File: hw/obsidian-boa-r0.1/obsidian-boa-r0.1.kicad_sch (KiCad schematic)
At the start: 79 parts, among them J1 USB_C, J2 PROG, P0 0, P1 1, P10 10, P11 11, P12 12, P13 13, P14 14, P15 15, P16 16, P17 17, P18 18, P19 19, P2 2, P20 20, P21 21, P22 22, P23 23, P24 GND, P25 GND, P26 GND, P27 3V3, P28 3V3, P29 VIN, P3 3, P30 CDONE, P31 CRESET, P32 UP, P33 UP, P34 UP, P35 UP, P4 4, P5 5, P6 6, P7 7, P8 8, P9 9, SW1 TACT, U1 USBLC6-2, U2 W25Q32JVSS, U3 ESP32-S2, U4 W25Q32JVSS, U5 TPS62290, Y1 40MHz

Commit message: hw.r0d1: Tidy up schematic, plan out layout on PCB
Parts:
- removed JP5: Jumper, pkl_jumpers:J_NC_0603_30, symbol icebreaker-bitsy-rescue:pkl_jumper_nc-pkl_misc
- removed R6: 1k5, pkl_dipol:R_0402, symbol icebreaker-bitsy-rescue:pkl_R_Small-pkl_device
- removed R9: 10k, pkl_dipol:R_Array_Convex_4x0402, symbol icebreaker-bitsy-rescue:pkl_R4_Small-pkl_device
- removed RN1: R_Network04_Split, Resistor_SMD:R_Array_Convex_4x0402, symbol Device:R_Network04_Split
- added C13, C15: 100n, Capacitor_SMD:C_0402_1005Metric, symbol icebreaker-bitsy-rescue:pkl_C_Small-pkl_device
- added C14, C8: 10u, Capacitor_SMD:C_0603_1608Metric, symbol icebreaker-bitsy-rescue:pkl_C-pkl_device
- added FB1, FB2, FB3: 240R, Inductor_SMD:L_0402_1005Metric, symbol Device:Ferrite_Bead_Small
- added L2: L_Small, Inductor_SMD:L_0402_1005Metric, symbol Device:L_Small
- added RN1: 10k, Resistor_SMD:R_Array_Convex_4x0402, symbol Device:R_Pack04_Split
- C1, C12, C2, C3, C4, C9: footprint pkl_dipol:C_0402 -> Capacitor_SMD:C_0402_1005Metric
- C10, C11: value 100n -> TBD; footprint pkl_dipol:C_0402 -> Capacitor_SMD:C_0402_1005Metric
- C19: footprint pkl_dipol:C_0603 -> Capacitor_SMD:C_0603_1608Metric
- D1, D2, D3: footprint pkl_dipol:D_0603 -> obsidian-boa:LED_0603_1608Metric_Compact; symbol icebreaker-bitsy-rescue:pkl_Led_Small-pkl_device -> Device:LED_ALT
- JP1: footprint pkl_jumpers:J_NC_0603_40 -> Jumper:SolderJumper-2_P1.3mm_Bridged2Bar_RoundedPad1.0x1.5mm
- R1, R10, R11, R12, R13, R2, R3, R4, R5: footprint pkl_dipol:R_0402 -> Resistor_SMD:R_0402_1005Metric
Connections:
- net VCCIO_0 is gone; now on an unnamed net: C10.1
- net VCCIO_2 is gone; now on net +3V3: R10.2
- net +3V3: now also FB1.1, FB2.1, FB3.1, RN1.5 (R4.2), RN1.6 (R3.2), RN1.7 (R2.2), RN1.8 (R1.2); no longer C11.1, C19.1, C9.1, U3.1 (VDDA), U3.20 (VDD3P3_RTC), U3.27 (VDD3P3_RTC_IO), U3.3 (VDD3P3), U3.30 (VDD_SPI), U3.4 (VDD3P3), U3.45 (VDD3P3_CPU), U3.51 (VDDA), U3.54 (VDDA)
- net CDONE: no longer D3.A, R13.1
- net GND: now also Y1.2, Y1.4, C13.2, C14.2, C15.2, C8.2; no longer D3.C
- net IOB_13b-~LEDG: now also D2.1 (K); no longer D2.C
- net IOT_36b-~LEDR: now also D1.1 (K); no longer D1.C
- net RAM_~CS: now also RN1.2 (R2.1)
- net SPI_SCK: now also RN1.3 (R3.1)
- net SPI_~CS: now also RN1.1 (R1.1)
- net USB_N: now also U3.25 (GPIO19)
- net USB_P: now also U3.26 (GPIO20)
- net ~CRESET: now also RN1.4 (R4.1)
- net at R12.1: now also D2.2 (A); no longer D2.A
- net at R11.1: now also D1.2 (A); no longer D1.A
- net at U3.2 (LNA_IN): now also L2.1
- net at AE1.1 (A): now also C11.1, L2.2
- new net: C19.1, C9.1, FB1.2, U3.20 (VDD3P3_RTC), U3.27 (VDD3P3_RTC_IO), U3.30 (VDD_SPI), U3.45 (VDD3P3_CPU)
- new net: D3.2 (A), R13.1
- new net: C13.1, C8.1, FB3.2, U3.1 (VDDA), U3.51 (VDDA), U3.54 (VDDA)
- new net: C14.1, C15.1, FB2.2, U3.3 (VDD3P3), U3.4 (VDD3P3)
- new net IOB_13b-~LEDB: D3.1 (K)
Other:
- note removed: "3V3 VReg"
- note removed: "Using same values as STM32F1 spec"
- moved on the sheet: AE1, C12, C19, C3, C4, C9, R11, R12, R13, R4, R5, Y1

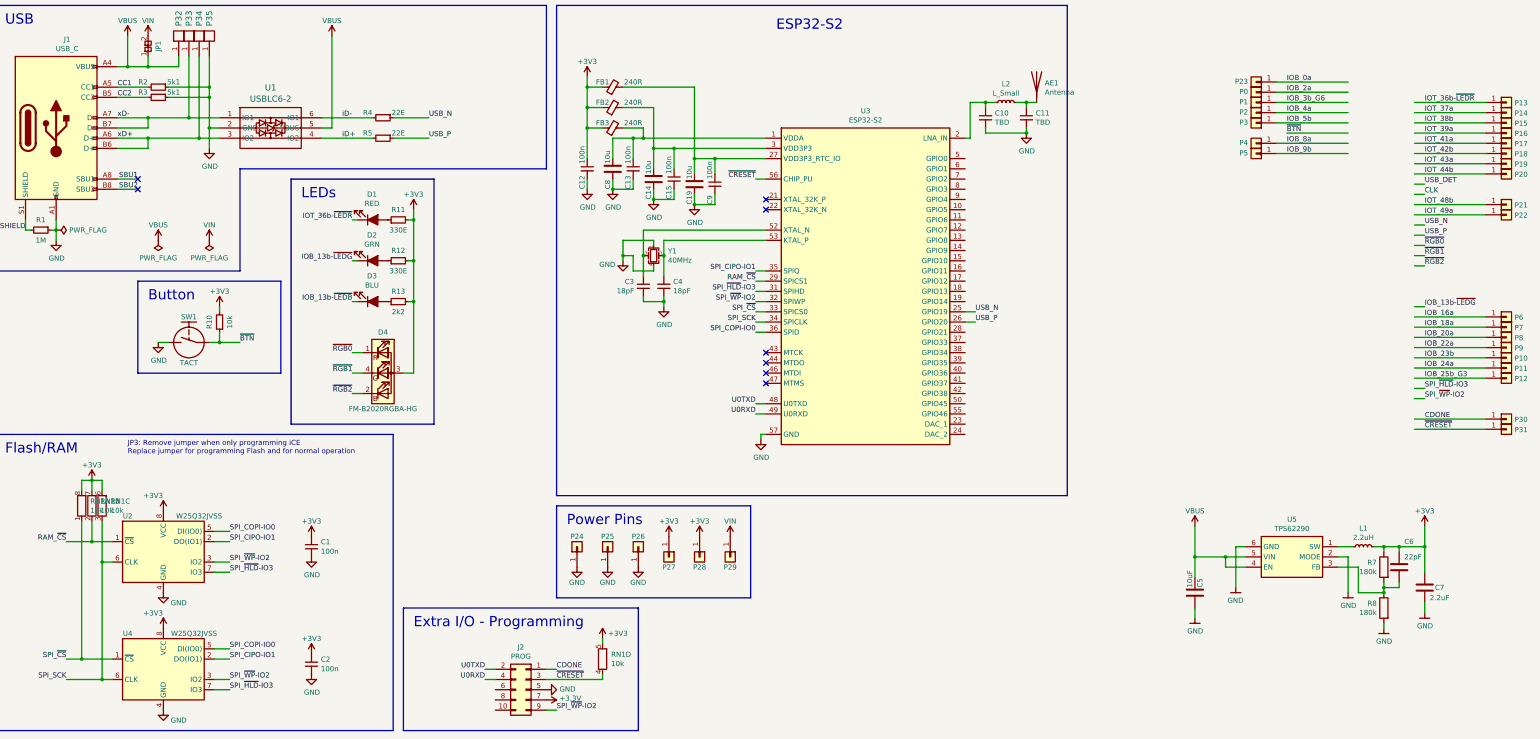
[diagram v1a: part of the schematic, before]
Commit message: hw.r0d1: Update routing and layout
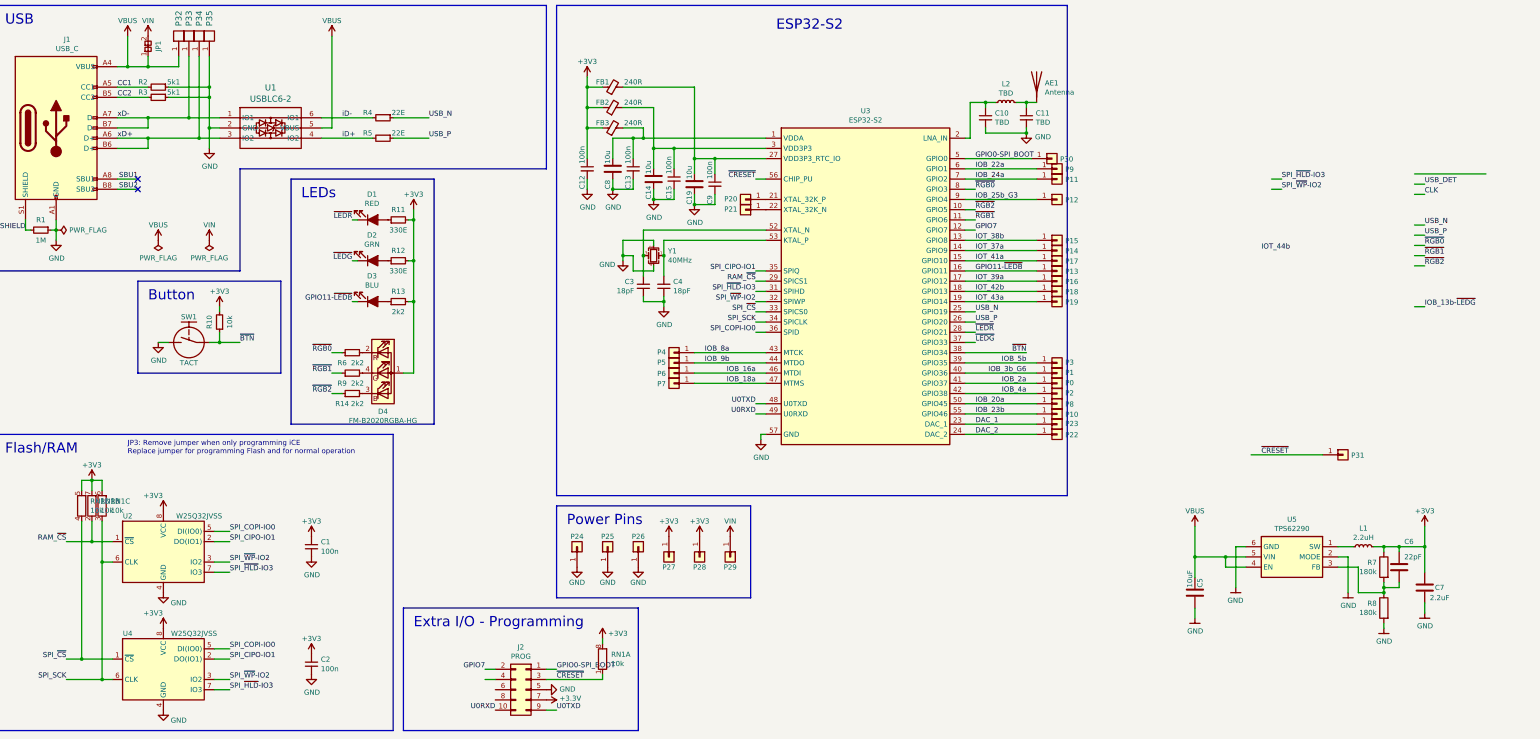
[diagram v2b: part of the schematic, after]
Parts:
- added R14, R6, R9: 2k2, Resistor_SMD:R_0402_1005Metric, symbol icebreaker-bitsy-rescue:pkl_R_Small-pkl_device
- D4: footprint pkl_led:LED_TRI_2020 -> LED_SMD:LED_Lumex_SML-LX0303SIUPGUSB; symbol icebreaker-bitsy-rescue:pkl_LED_RBAG-pkl_device -> Device:LED_ARBG
- L2: value L_Small -> TBD
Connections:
- net CDONE is gone; now on net GPIO0-SPI_BOOT: J2.1 (Pin_1), P30.1 (Pin_1)
- net IOB_0a is gone; now on net DAC_1: P23.1 (Pin_1)
- net IOB_13b-~LEDB is gone; now on net GPIO11-~LEDB: D3.1 (K)
- net IOT_48b is gone; now on an unnamed net: P21.1 (Pin_1)
- net IOT_49a is gone; now on net DAC_2: P22.1 (Pin_1)
- net +3V3: now also D4.1 (A); no longer D4.3 (A)
- net IOB_13b-~LEDG: no longer D2.1 (K)
- net IOB_16a: now also U3.46 (MTDI)
- net IOB_18a: now also U3.47 (MTMS)
- net IOB_20a: now also U3.50 (GPIO45)
- net IOB_22a: now also U3.6 (GPIO1)
- net IOB_23b: now also U3.55 (GPIO46)
- net IOB_24a: now also U3.7 (GPIO2)
- net IOB_25b_G3: now also U3.9 (GPIO4)
- net IOB_2a: now also U3.41 (GPIO37)
- net IOB_3b_G6: now also U3.40 (GPIO36)
- net IOB_4a: now also U3.42 (GPIO38)
- net IOB_5b: now also U3.39 (GPIO35)
- net IOB_8a: now also U3.43 (MTCK)
- net IOB_9b: now also U3.44 (MTDO)
- net IOT_37a: now also U3.14 (GPIO9)
- net IOT_38b: now also U3.13 (GPIO8)
- net IOT_39a: now also U3.17 (GPIO12)
- net IOT_41a: now also U3.15 (GPIO10)
- net IOT_42b: now also U3.18 (GPIO13)
- net IOT_43a: now also U3.19 (GPIO14)
- net IOT_44b: no longer P20.1 (Pin_1)
- net SPI_~CS: now also RN1.4 (R4.1); no longer RN1.1 (R1.1)
- net SPI_~WP~-IO2: no longer J2.9 (Pin_9)
- net U0RXD: now also J2.10 (Pin_10); no longer J2.4 (Pin_4)
- net U0TXD: now also J2.9 (Pin_9); no longer J2.2 (Pin_2)
- net ~BTN: now also U3.38 (GPIO34)
- net ~CRESET: now also RN1.1 (R1.1); no longer RN1.4 (R4.1)
- net ~RGB0: now also U3.8 (GPIO3), R6.1; no longer D4.1 (RK)
- net ~RGB1: now also U3.11 (GPIO6), R9.1; no longer D4.4 (GK)
- net ~RGB2: now also U3.10 (GPIO5), R14.1; no longer D4.2 (BK)
- net GPIO7: now reaches U3.12 (GPIO7)
- net GPIO7: now also J2.2 (Pin_2)
- net GPIO11-~LEDB: now reaches U3.16 (GPIO11)
- net GPIO11-~LEDB: now also P13.1 (Pin_1)
- net at U3.21 (XTAL_32K_P): now also P20.1 (Pin_1)
- net DAC_1: now reaches U3.23 (DAC_1)
- net DAC_2: now reaches U3.24 (DAC_2)
- net ~LEDR: now reaches U3.28 (GPIO21)
- net ~LEDR: now also D1.1 (K)
- net ~LEDG: now reaches U3.37 (GPIO33)
- net ~LEDG: now also D2.1 (K)
- net GPIO0-SPI_BOOT: now reaches U3.5 (GPIO0)
- removed net IOT_36b-~LEDR: D1.1 (K), P13.1 (Pin_1)
- new net: D4.2 (RK), R6.2
- new net: D4.3 (BK), R14.2
- new net: D4.4 (GK), R9.2
- no-connect marks 8 -> 2
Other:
- moved on the sheet: P0, P1, P10, P11, P12, P13, P14, P15, P16, P17, P18, P19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

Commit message: hw.r0d1: Complete first pass of layout and routing
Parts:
- AE1: symbol Device:Antenna -> Device:Antenna_Shield
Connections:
- net GND: now also AE1.2 (Shield)
- net SPI_CIPO-IO1: now also J2.6 (Pin_6)
- net SPI_COPI-IO0: now also J2.8 (Pin_8)
- net SPI_SCK: now also J2.4 (Pin_4)
- net GPIO15: now reaches P20.1 (Pin_1), U3.21 (XTAL_32K_P)
- net GPIO16: now reaches P21.1 (Pin_1), U3.22 (XTAL_32K_N)
- net DAC_1 renamed GPIO17-DAC_1
- net DAC_2 renamed GPIO18-DAC_2
- net GPIO0-SPI_BOOT renamed GPIO0-BOOT
- net IOB_16a renamed GPIO41
- net IOB_18a renamed GPIO42
- net IOB_20a renamed GPIO45
- net IOB_22a renamed GPIO1
- net IOB_23b renamed GPIO46
- net IOB_24a renamed GPIO2
- net IOB_25b_G3 renamed GPIO4
- net IOB_2a renamed GPIO37
- net IOB_3b_G6 renamed GPIO36
- net IOB_4a renamed GPIO38
- net IOB_5b renamed GPIO35
- net IOB_8a renamed GPIO39
- net IOB_9b renamed GPIO40
- net IOT_37a renamed GPIO9
- net IOT_38b renamed GPIO8
- net IOT_39a renamed GPIO12
- net IOT_41a renamed GPIO10
- net IOT_42b renamed GPIO13
- net IOT_43a renamed GPIO14
- net ~BTN renamed GPIO34-~BTN
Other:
- note removed: "JP3: Remove jumper when only programming iCE Replace jumper for programming Flash and for normal operation"
- moved on the sheet: C10, C11, C12, C13, C14, C15, C19, C3, C4, C5, C6, C7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
